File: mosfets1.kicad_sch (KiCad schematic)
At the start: 38 parts, among them Q10 IXFK300N20X3, Q11 IXFK300N20X3, Q12 IXFK300N20X3, Q13 IXFK300N20X3, Q8 IXFK300N20X3, Q9 IXFK300N20X3, U15 ACS781xLRTR-150B, U16 ACS781xLRTR-150B, U17 ACS781xLRTR-150B

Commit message: - some layout work
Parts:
- removed C77: 100n, Capacitor_SMD:C_0805_2012Metric, symbol Device:C
- removed C78: 1u, Capacitor_SMD:C_0805_2012Metric, symbol Device:C
- removed C79: 4n7, Capacitor_SMD:C_0805_2012Metric, symbol Device:C
- removed R58: 1k, Resistor_SMD:R_0805_2012Metric, symbol Device:R
- removed U17: ACS781xLRTR-150B, Sensor_Current:Allegro_PSOF-7_4.8x6.4mm_P1.60mm, symbol Sensor_Current:ACS781xLRTR-150B
- C68, C69, C70, C71, C72, C73: footprint Capacitor_SMD:C_2220_5650Metric -> Capacitor_SMD:C_2220_5750Metric
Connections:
- no-connect marks 6 -> 4

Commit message: - layout almost finished
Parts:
- removed C7, C74: 100n, Capacitor_SMD:C_0805_2012Metric, symbol Device:C
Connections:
- net U renamed U1
- net U_GH renamed U1_GH
- net U_GL renamed U1_GL
- net U_I renamed U1_I
- net U_VP renamed U1_VP
- net V renamed V1
- net V_GH renamed V1_GH
- net V_GL renamed V1_GL
- net V_I renamed V1_I
- net V_VP renamed V1_VP
- net W_GH renamed W1_GH
- net W_GL renamed W1_GL
- net W_VP renamed W1
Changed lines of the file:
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@@
   (junction (at 140.97 177.8) (diameter 0) (color 0 0 0 0)
   )
-  (junction (at 227.33 137.16) (diameter 0) (color 0 0 0 0)
-  )
   (junction (at 115.57 177.8) (diameter 0) (color 0 0 0 0)
   )
@@
   (junction (at 87.63 177.8) (diameter 0) (color 0 0 0 0)
   )
-  (junction (at 52.07 137.16) (diameter 0) (color 0 0 0 0)
-  )
   (junction (at 87.63 185.42) (diameter 0) (color 0 0 0 0)
   )
@@
   )
   (junction (at 139.7 92.71) (diameter 0) (color 0 0 0 0)
-  )
-  (junction (at 139.7 137.16) (diameter 0) (color 0 0 0 0)
   )
   (junction (at 154.94 87.63) (diameter 0) (color 0 0 0 0)
@@
     (stroke (width 0) (type default))
   )
-  (wire (pts (xy 210.82 137.16) (xy 227.33 137.16))
-    (stroke (width 0) (type default))
-  )
-  (wire (pts (xy 62.23 87.63) (xy 67.31 87.63))
-    (stroke (width 0) (type default))
-  )
   (wire (pts (xy 67.31 87.63) (xy 72.39 87.63))
     (stroke (width 0) (type default))
   )
-  (wire (pts (xy 123.19 137.16) (xy 139.7 137.16))
-    (stroke (width 0) (type default))
-  )
   (wire (pts (xy 87.63 185.42) (xy 93.98 185.42))
     (stroke (width 0) (type default))
@@
     (stroke (width 0) (type default))
   )
+  (wire (pts (xy 227.33 92.71) (xy 229.87 92.71))
+    (stroke (width 0) (type default))
+  )
   (wire (pts (xy 52.07 137.16) (xy 52.07 125.73))
     (stroke (width 0) (type default))
@@
     (stroke (width 0) (type default))
   )
-  (wire (pts (xy 36.83 137.16) (xy 52.07 137.16))
-    (stroke (width 0) (type default))
-  )
   (wire (pts (xy 139.7 92.71) (xy 123.19 92.71))
     (stroke (width 0) (type default))
@@
     (stroke (width 0) (type default))
   )
-  (hierarchical_label "W_VS" (shape input) (at 210.82 137.16 180) (fields_autoplaced)
+  (hierarchical_label "U1_GL" (shape input) (at 36.83 120.65 180) (fields_autoplaced)
     (effects (font (size 1.524 1.524)) (justify right))
   )
-  (hierarchical_label "U_GL" (shape input) (at 36.83 120.65 180) (fields_autoplaced)
+  (hierarchical_label "W1_GL" (shape input) (at 210.82 120.65 180) (fields_autoplaced)
     (effects (font (size 1.524 1.524)) (justify right))
   )
-  (hierarchical_label "W_GL" (shape input) (at 210.82 120.65 180) (fields_autoplaced)
+  (hierarchical_label "V1_GL" (shape input) (at 123.19 120.65 180) (fields_autoplaced)
     (effects (font (size 1.524 1.524)) (justify right))
   )
-  (hierarchical_label "V_GL" (shape input) (at 123.19 120.65 180) (fields_autoplaced)
+  (hierarchical_label "U1" (shape output) (at 57.15 97.79 180) (fields_autoplaced)
     (effects (font (size 1.524 1.524)) (justify right))
   )
-  (hierarchical_label "U" (shape output) (at 57.15 97.79 180) (fields_autoplaced)
+  (hierarchical_label "U1_VP" (shape output) (at 36.83 92.71 180) (fields_autoplaced)
     (effects (font (size 1.524 1.524)) (justify right))
   )
-  (hierarchical_label "U_VS" (shape input) (at 36.83 137.16 180) (fields_autoplaced)
+  (hierarchical_label "U1_I" (shape input) (at 85.09 95.25 0) (fields_autoplaced)
+    (effects (font (size 1.27 1.27)) (justify left))
+  )
+  (hierarchical_label "U1_GH" (shape input) (at 36.83 66.04 180) (fields_autoplaced)
     (effects (font (size 1.524 1.524)) (justify right))
   )
-  (hierarchical_label "U_VP" (shape output) (at 36.83 92.71 180) (fields_autoplaced)
+  (hierarchical_label "V1_I" (shape input) (at 172.72 95.25 0) (fields_autoplaced)
+    (effects (font (size 1.27 1.27)) (justify left))
+  )
+  (hierarchical_label "W1_GH" (shape input) (at 210.82 66.04 180) (fields_autoplaced)
     (effects (font (size 1.524 1.524)) (justify right))
   )
-  (hierarchical_label "U_I" (shape input) (at 85.09 95.25 0) (fields_autoplaced)
-    (effects (font (size 1.27 1.27)) (justify left))
-  )
-  (hierarchical_label "U_GH" (shape input) (at 36.83 66.04 180) (fields_autoplaced)
+  (hierarchical_label "V1" (shape output) (at 144.78 97.79 180) (fields_autoplaced)
     (effects (font (size 1.524 1.524)) (justify right))
   )
-  (hierarchical_label "V_I" (shape input) (at 172.72 95.25 0) (fields_autoplaced)
-    (effects (font (size 1.27 1.27)) (justify left))
-  )
-  (hierarchical_label "W_GH" (shape input) (at 210.82 66.04 180) (fields_autoplaced)
+  (hierarchical_label "V1_GH" (shape input) (at 123.19 66.04 180) (fields_autoplaced)
     (effects (font (size 1.524 1.524)) (justify right))
   )
-  (hierarchical_label "V" (shape output) (at 144.78 97.79 180) (fields_autoplaced)
+  (hierarchical_label "V1_VP" (shape output) (at 123.19 92.71 180) (fields_autoplaced)
     (effects (font (size 1.524 1.524)) (justify right))
   )
-  (hierarchical_label "V_VS" (shape input) (at 123.19 137.16 180) (fields_autoplaced)
+  (hierarchical_label "W1_VP" (shape output) (at 210.82 92.71 180) (fields_autoplaced)
     (effects (font (size 1.524 1.524)) (justify right))
   )
-  (hierarchical_label "V_GH" (shape input) (at 123.19 66.04 180) (fields_autoplaced)
-    (effects (font (size 1.524 1.524)) (justify right))
-  )
-  (hierarchical_label "V_VP" (shape output) (at 123.19 92.71 180) (fields_autoplaced)
-    (effects (font (size 1.524 1.524)) (justify right))
-  )
-  (hierarchical_label "W_VP" (shape output) (at 210.82 92.71 180) (fields_autoplaced)
-    (effects (font (size 1.524 1.524)) (justify right))
+  (hierarchical_label "W1" (shape output) (at 229.87 92.71 0) (fields_autoplaced)
+    (effects (font (size 1.524 1.524)) (justify left))
   )
   (symbol (lib_id "power:+BATT") (at 227.33 43.18 0) (unit 1)
@@
     )
   )
-  (symbol (lib_id "Device:C") (at 62.23 83.82 0) (mirror x) (unit 1)
-    (in_bom yes) (on_board yes) (dnp no)
-    (property "Reference" "C7" (at 59.309 82.6516 0)
-      (effects (font (size 1.27 1.27)) (justify right))
-    )
-    (property "Value" "100n" (at 59.309 84.963 0)
-      (effects (font (size 1.27 1.27)) (justify right))
-    )
-    (property "Footprint" "Capacitor_SMD:C_0805_2012Metric" (at 63.1952 80.01 0)
-      (effects (font (size 1.27 1.27)) hide)
-    )
-    (property "Datasheet" "~" (at 62.23 83.82 0)
-      (effects (font (size 1.27 1.27)) hide)
-    )
-    (pin "1")
-    (pin "2")
-    (instances
-      (project "HSWR"
-        (path "/51094070-255e-40e7-bed5-d199e288e5dd/e2e9d5db-9823-43ca-86ac-002f871f7258"
-          (reference "C7") (unit 1)
-        )
-        (path "/51094070-255e-40e7-bed5-d199e288e5dd/00000000-0000-0000-0000-00005895e67a"
-          (reference "C33") (unit 1)
-        )
-      )
-    )
-  )
   (symbol (lib_id "Device:C") (at 72.39 83.82 0) (unit 1)
     (in_bom yes) (on_board yes) (dnp no)
@@
     )
   )
-  (symbol (lib_id "power:GND") (at 62.23 80.01 180) (unit 1)
-    (in_bom yes) (on_board yes) (dnp no)
-    (property "Reference" "#PWR012" (at 62.23 73.66 0)
-      (effects (font (size 1.27 1.27)) hide)
-    )
-    (property "Value" "GND" (at 62.103 75.6158 0)
-      (effects (font (size 1.27 1.27)))
-    )
-    (property "Footprint" "" (at 62.23 80.01 0)
-      (effects (font (size 1.27 1.27)) hide)
-    )
-    (property "Datasheet" "" (at 62.23 80.01 0)
-      (effects (font (size 1.27 1.27)) hide)
-    )
-    (pin "1")
-    (instances
-      (project "HSWR"
-        (path "/51094070-255e-40e7-bed5-d199e288e5dd/e2e9d5db-9823-43ca-86ac-002f871f7258"
-          (reference "#PWR012") (unit 1)
-        )
-        (path "/51094070-255e-40e7-bed5-d199e288e5dd/00000000-0000-0000-0000-00005895e67a"
-          (reference "#PWR0104") (unit 1)
-        )
-      )
-    )
-  )
   (symbol (lib_id "power:GND") (at 72.39 80.01 180) (unit 1)
     (in_bom yes) (on_board yes) (dnp no)
@@
     )
   )
-  (symbol (lib_id "Device:C") (at 149.86 83.82 0) (mirror x) (unit 1)
-    (in_bom yes) (on_board yes) (dnp no)
-    (property "Reference" "C74" (at 146.939 82.6516 0)
-      (effects (font (size 1.27 1.27)) (justify right))
-    )
-    (property "Value" "100n" (at 146.939 84.963 0)
-      (effects (font (size 1.27 1.27)) (justify right))
-    )
-    (property "Footprint" "Capacitor_SMD:C_0805_2012Metric" (at 150.8252 80.01 0)
-      (effects (font (size 1.27 1.27)) hide)
-    )
-    (property "Datasheet" "~" (at 149.86 83.82 0)
-      (effects (font (size 1.27 1.27)) hide)
-    )
-    (pin "1")
-    (pin "2")
-    (instances
-      (project "HSWR"
-        (path "/51094070-255e-40e7-bed5-d199e288e5dd/e2e9d5db-9823-43ca-86ac-002f871f7258"
-          (reference "C74") (unit 1)
-        )
-        (path "/51094070-255e-40e7-bed5-d199e288e5dd/00000000-0000-0000-0000-00005895e67a"
-          (reference "C47") (unit 1)
-        )
-      )
-    )
-  )
   (symbol (lib_id "Device:C") (at 160.02 83.82 0) (unit 1)
     (in_bom yes) (on_board yes) (dnp no)
@@
         )
       )
-    )
-  )
-  (symbol (lib_id "power:GND") (at 149.86 80.01 180) (unit 1)
-    (in_bom yes) (on_board yes) (dnp no)
-    (property "Reference" "#PWR093" (at 149.86 73.66 0)
-      (effects (font (size 1.27 1.27)) hide)
-    )
-    (property "Value" "GND" (at 149.733 75.6158 0)
-      (effects (font (size 1.27 1.27)))
-    )
-    (property "Footprint" "" (at 149.86 80.01 0)
-      (effects (font (size 1.27 1.27)) hide)
-    )
-    (property "Datasheet" "" (at 149.86 80.01 0)
-      (effects (font (size 1.27 1.27)) hide)
-    )
-    (pin "1")
-    (instances
-      (project "HSWR"
-        (path "/51094070-255e-40e7-bed5-d199e288e5dd/e2e9d5db-9823-43ca-86ac-002f871f7258"
-          (reference "#PWR093") (unit 1)
-        )
-        (path "/51094070-255e-40e7-bed5-d199e288e5dd/00000000-0000-0000-0000-00005895e67a"
-          (reference "#PWR0113") (unit 1)
-        )
-      )

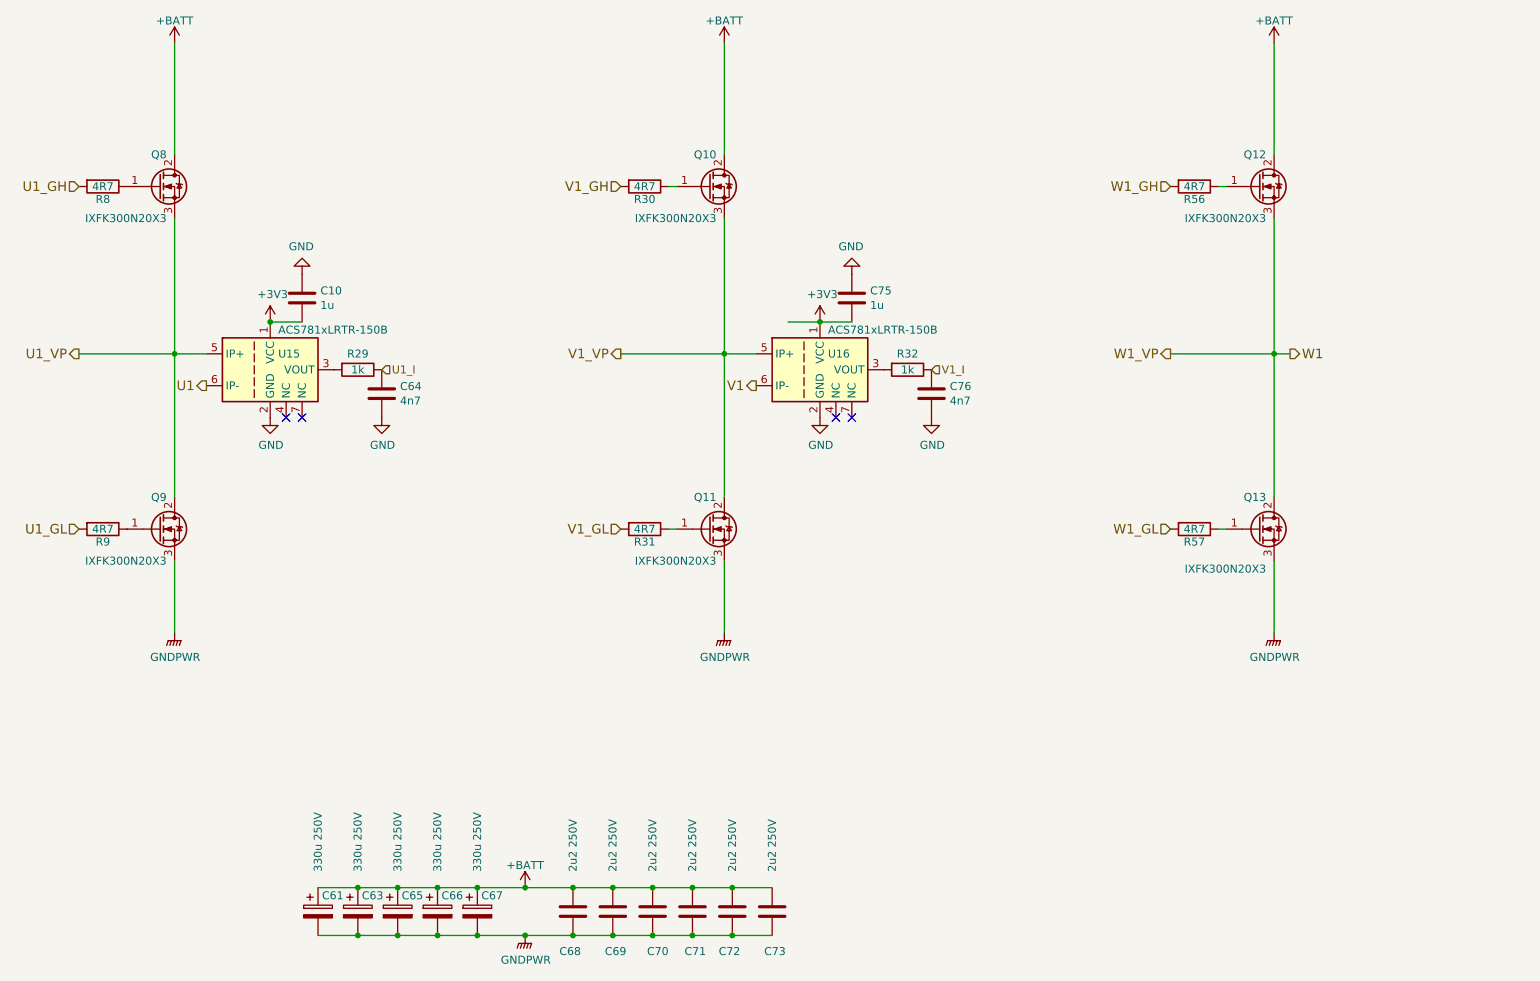
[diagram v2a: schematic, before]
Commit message: - fixed missing 3V3 trace on USB isolator
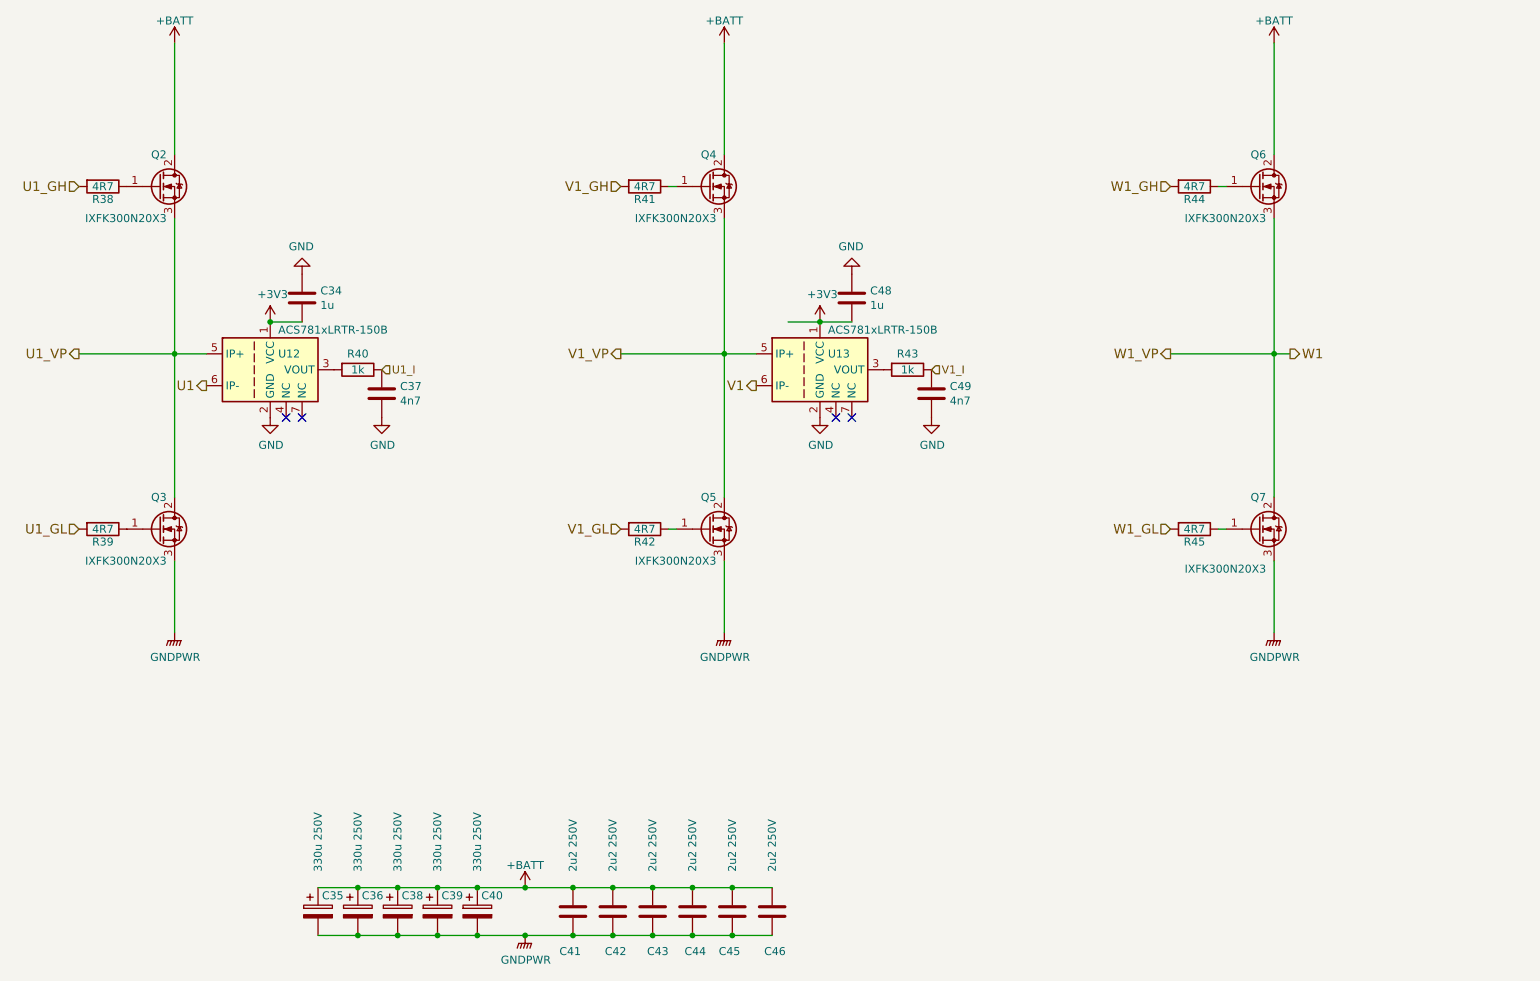
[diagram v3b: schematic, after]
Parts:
- renumbered C10 to C34, C61 to C35, C63 to C36, C64 to C37, C65 to C38, C66 to C39, C67 to C40, C68 to C41, C69 to C42, C70 to C43, C71 to C44, C72 to C45, C73 to C46, C75 to C48, C76 to C49, Q8 to Q2, Q9 to Q3, Q10 to Q4, Q11 to Q5, Q12 to Q6, Q13 to Q7, R8 to R38, R9 to R39, R29 to R40, R30 to R41, R31 to R42, R32 to R43, R56 to R44, R57 to R45, U15 to U12, U16 to U13
